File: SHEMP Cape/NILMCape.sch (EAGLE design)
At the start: 26 parts, among them U1 ADS8568_PM_64, U2 ACS756KCA-050B-PFF-T, U3 LTC6082, U4 LTC6082, U5 LM2687_DGK_8

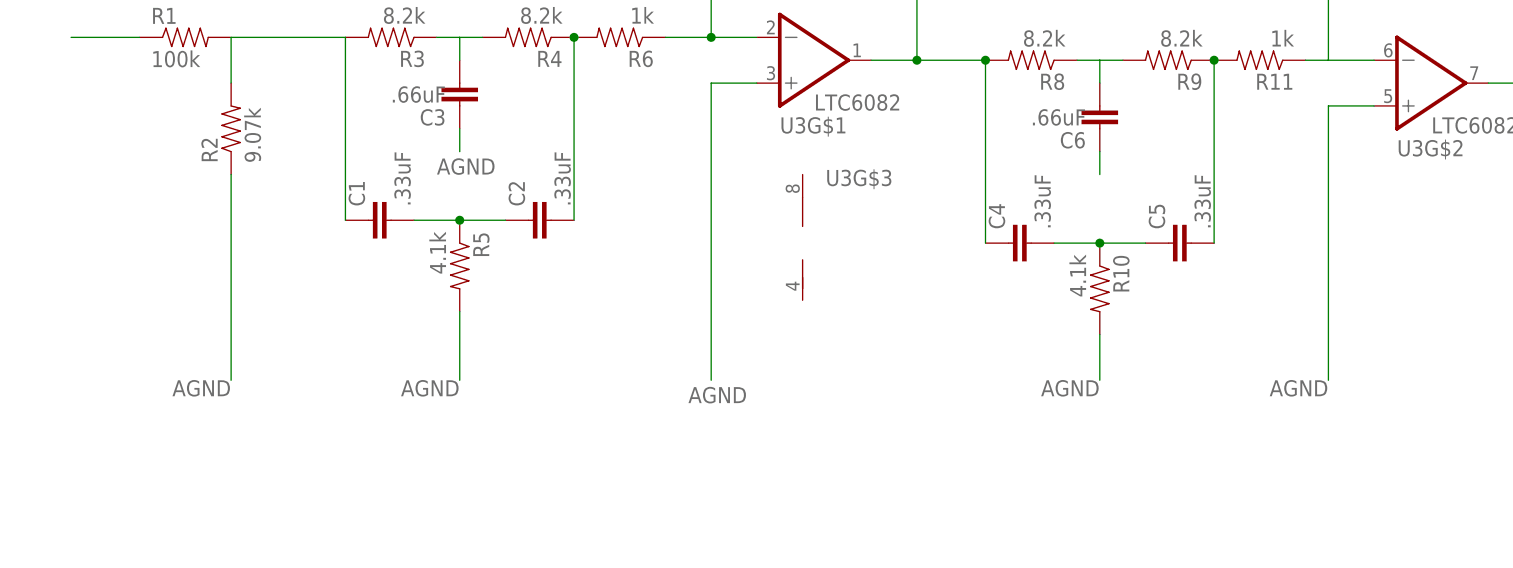
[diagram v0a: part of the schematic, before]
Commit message: Added Frequency Response
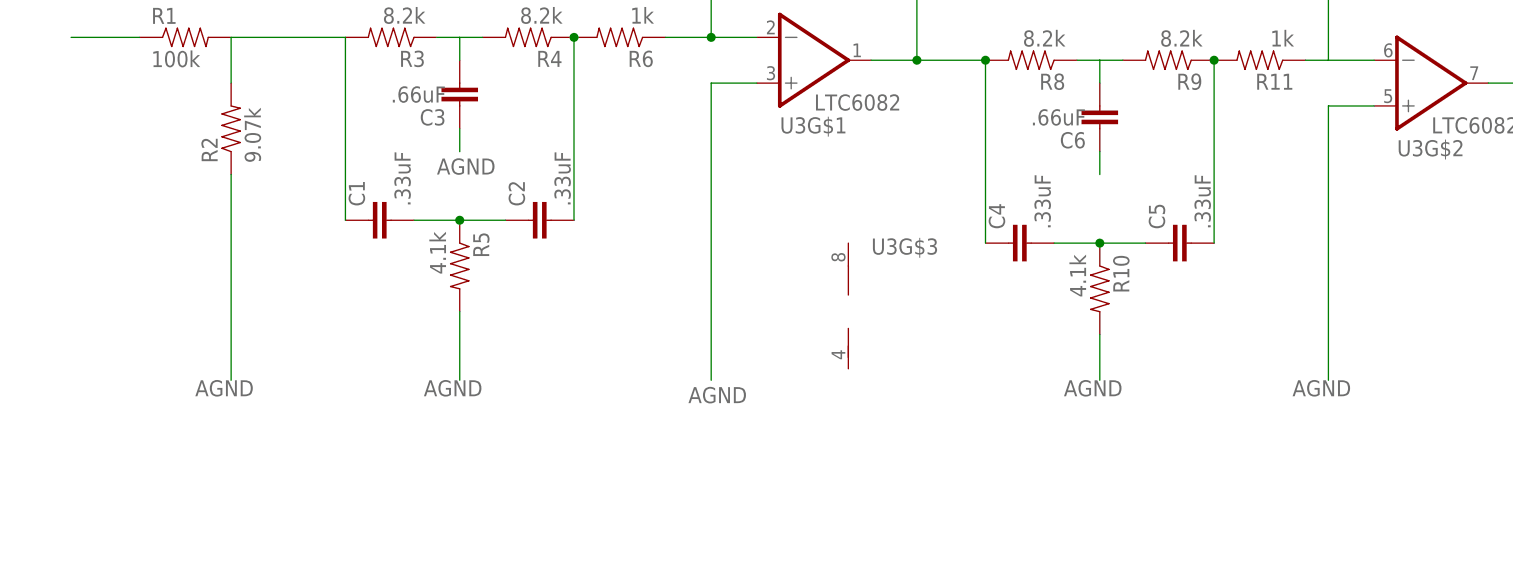
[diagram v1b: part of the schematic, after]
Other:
- moved on the sheet: U3G$3
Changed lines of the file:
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@@
 <?xml version="1.0" encoding="utf-8"?>
 <!DOCTYPE eagle SYSTEM "eagle.dtd">
-<eagle version="6.4">
+<eagle version="6.5.0">
 <drawing>
 <settings>
@@
 <instance part="U3" gate="G$1" x="208.28" y="104.14" rot="MR180"/>
 <instance part="U3" gate="G$2" x="276.86" y="101.6" rot="MR180"/>
-<instance part="U3" gate="G$3" x="208.28" y="83.82"/>
+<instance part="U3" gate="G$3" x="213.36" y="76.2"/>
 <instance part="U2" gate="A" x="38.1" y="223.52"/>
 <instance part="U2" gate="B" x="68.58" y="220.98" rot="R90"/>
@@
 <pinref part="R2" gate="G$1" pin="1"/>
 <wire x1="144.78" y1="91.44" x2="144.78" y2="68.58" width="0.1524" layer="91"/>
-<label x="144.78" y="68.58" size="1.778" layer="95" rot="R180"/>
+<label x="147.32" y="68.58" size="1.778" layer="95" rot="R180"/>
 </segment>
 <segment>
 <pinref part="R5" gate="G$1" pin="2"/>
 <wire x1="170.18" y1="76.2" x2="170.18" y2="68.58" width="0.1524" layer="91"/>
-<label x="170.18" y="68.58" size="1.778" layer="95" rot="R180"/>
+<label x="172.72" y="68.58" size="1.778" layer="95" rot="R180"/>
 </segment>
 <segment>
@@
 <pinref part="R10" gate="G$1" pin="2"/>
 <wire x1="241.3" y1="73.66" x2="241.3" y2="68.58" width="0.1524" layer="91"/>
-<label x="241.3" y="68.58" size="1.778" layer="95" rot="R180"/>
+<label x="243.84" y="68.58" size="1.778" layer="95" rot="R180"/>
 </segment>
 <segment>
@@
 <wire x1="271.78" y1="99.06" x2="266.7" y2="99.06" width="0.1524" layer="91"/>
 <wire x1="266.7" y1="99.06" x2="266.7" y2="68.58" width="0.1524" layer="91"/>
-<label x="266.7" y="68.58" size="1.778" layer="95" rot="R180"/>
-</segment>
-</net>
+<label x="269.24" y="68.58" size="1.778" layer="95" rot="R180"/>
+</segment>
+</net>

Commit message: Split rail work, finished filtering stage.
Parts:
- removed R10: 4.1k, SensorCape:RESISTOR0805-RES
- removed R6: 1k, SensorCape:RESISTOR0805-RES
- added C10, C9: .33uF, SensorCape:CAP0805
- added C7, C8: 1uF, SensorCape:CAP0805
- added R13, R14: 8.2k, SensorCape:RESISTOR0805-RES
- added U$2: TPS84259_RKG_41, SensorCape:TPS84259_RKG_41
- added U$3: TPS7A4700_RGW_20, SensorCape:TPS7A4700_RGW_20
- added U6: TPS7A3301_RGW_20, SensorCape:TPS7A3301_RGW_20
- C3, C6: value .66uF -> .33uF
- R1: value 100k -> 1k
- R11: value 1k -> 15k
- R12: value 20k -> 1k
- R2: value 9.07k -> 8.2k
- R5: value 4.1k -> 8.2k
- R7: value 10k -> 1k
- U3, U4: value LTC6082 -> TLC2272A_D_8; device SensorCape:LTC6082 -> SensorCape:TLC2272A_D_8
- U5: value LM2687_DGK_8 -> TPS84250_RKG_41; device SensorCape:LM2687_DGK_8 -> SensorCape:TPS84250_RKG_41
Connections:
- removed net AVDD: U$1.SYS_5V@1, U$1.SYS_5V@2
- removed net DGND: U$1.GND@1, U$1.GND@2, U$1.GND@3, U$1.GND@4, U$1.GND@5, U$1.GND@6, U$1.GND@7, U$1.GND@8
- removed net DVDD: U$1.VDD_3V3EXP@1, U$1.VDD_3V3EXP@2
- removed net N$1: R1.1
- removed net N$14: C6.2, R8.1, R9.2
- removed net N$5: C2.2, R4.1, R6.2
- new net N$17: C7.1, U3.1IN-, U3.1OUT
- new net N$30: C7.2, R1.2
- new net N$31: R1.1, R7.2, U3.2IN-
- new net N$32: R11.2, R12.1, U4.2IN-
- new net N$33: U4.2OUT
- net AGND: now also C10.1, C4.1, C9.1, R13.2, R14.2, R2.2, U3.2IN+, U4.2IN+; no longer R10.2, R2.1, U3G$1.+IN, U3G$2.+IN
- net HVDD: now also U3.VDD+, U4.VDD+; no longer U$1.VDD_5V@1, U$1.VDD_5V@2
- net HVSS: now also U3.VDD-/GND, U4.VDD-/GND; no longer U5.OUT
- net N$10: now also C5.1, U3.2OUT; no longer C4.1, R7.1, U3G$1.OUT
- net N$11: now also C5.2, C6.1, R13.1, R14.1; no longer R11.1, R12.2, U3G$2.-IN
- net N$13: now also C10.2, C9.2, R8.1, R9.2; no longer C4.2, C5.1, R10.1
- net N$15: now also C6.2, U4.1IN+; no longer C5.2, R11.2
- net N$16: now also C8.1, U4.1IN-, U4.1OUT; no longer C6.1
- net N$18: now also C8.2, R12.2; no longer R12.1, U3G$2.OUT
- net N$2: no longer R1.2, R2.2
- net N$3: now also R2.1
- net N$4: now also C4.2
- net N$9: now also C2.2, R4.1, U3.1IN+; no longer R6.1, R7.2, U3G$1.-IN
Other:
- note added: "This needs to be connected to the AC input"

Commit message: More schematic capture work.
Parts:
- removed U3, U4: TLC2272A_D_8, SensorCape:TLC2272A_D_8
- added C11: 1uF, SensorCape:CAP0805
- added C12: 4.7uF 50V, SensorCape:CAP1210
- added C13: 2.2uF 100V, SensorCape:CAP1210
- added C14: 22uF 100V, ASL:CAP_POLPTH1
- added C15, C16, C17, C18: 22uF 25V, SensorCape:CAP1210
- added R10, R6: 1k, SensorCape:RESISTOR0805-RES
- added R15: 174k, ASL:RESISTOR0805-RES
- added R16: 63.4k, ASL:RESISTOR0805-RES
- added U7: LP2950-33_KVU_3, SensorCape:LP2950-33_KVU_3
- added U9: TL074_PW_14, SensorCape:TL074_PW_14
- C10: value .33uF -> 1uF
- C7: value 1uF -> .33uF
- C8: value 1uF -> 4.7uF 50V; device SensorCape:CAP0805 -> SensorCape:CAP1210
- R1, R7: value 1k -> 8.2k
- R11: value 15k -> 178k; device SensorCape:RESISTOR0805-RES -> ASL:RESISTOR0805-RES
- R12: value 1k -> 0; device SensorCape:RESISTOR0805-RES -> ASL:RESISTOR0805-RES
- R13, R14: value 8.2k -> 1k
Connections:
- net N$2 renamed HOT_IN
- removed net N$15: C6.2, R9.1, U4.1IN+
- removed net N$16: C8.1, U4.1IN-, U4.1OUT
- removed net N$32: R11.2, R12.1, U4.2IN-
- removed net N$33: U4.2OUT
- new net GND: C12.2, C13.2, C14.-, C15.1, C16.1, C17.1, C18.1, C8.2, R11.2, U$2.GND
- new net HVSS_15D: C15.2, C16.2, C17.2, C18.2, U$2.VOUT
- new net N$1: C5.1, R1.2, R6.2, U9.2OUT
- new net N$14: C10.2, U9.3IN-, U9.3OUT
- new net N$34: C11.2, R10.2
- new net N$35: C11.1, U9.1IN-, U9.1OUT
- new net N$36: R15.1, R16.2, U$2.INH/UVLO
- new net N$37: R12.1, R16.1, U$2.A_VOUT
- new net N$5: R10.1, R6.1, U9.2IN-
- new net SIGNAL_TO_AA: R14.1, U9.4OUT
- new net VIN: C12.1, C13.1, C14.+, C8.1, R15.2, U$2.VIN
- net AGND: now also C7.1, R8.2, R9.2, U9.2IN+, U9.4IN+; no longer C10.1, R13.2, R14.2, U3.2IN+, U4.2IN+
- net HVDD: now also U9.VCC+; no longer U3.VDD+, U4.VDD+
- net HVSS: now also U9.VCC-; no longer U3.VDD-/GND, U4.VDD-/GND
- net N$10: now also C5.2, C6.1, R8.1, R9.1; no longer C5.1, R8.2, U3.2OUT
- net N$11: now also C7.2, C9.2, R1.1, R7.2; no longer C5.2, C6.1, R13.1, R14.1
- net N$13: now also C6.2, R7.1, U9.3IN+; no longer C10.2, C9.2, R8.1, R9.2
- net N$17: now also R13.2, R14.2, U9.4IN-; no longer C7.1, U3.1IN-, U3.1OUT
- net N$18: now also R11.1, U$2.VADJ; no longer C8.2, R12.2
- net N$30: now also C10.1, R13.1; no longer C7.2, R1.2
- net N$31: now also R12.2, U$2.RT; no longer R1.1, R7.2, U3.2IN-
- net N$9: now also U9.1IN+; no longer U3.1IN+
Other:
- note added: "60Hz Filter"
- note added: "SPLIT RAIL CLEAN/DIRTY AND LOGIC VOLTAGE SUPPLY"
- note removed: "This needs to be connected to the AC input"

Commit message: More schematic capture work.
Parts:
- added C19, C26, C31: 10nF, SensorCape:CAP0805
- added C20, C23, C25: 22uF, SensorCape:CAP1210
- added C21, C22, C24: 2.2uF 100V, SensorCape:CAP1210
- added C27: 27uF 100V, SensorCape:CAP_POLPTH1
- added C28, C30: 1uF, SensorCape:CAP0805
- added C29, C32: 47uF, SensorCape:CAP1210
- added C33: 10uF, SensorCape:CAP_POLPTH2
- added C34, C35, C36, C37, C38, C39, C40, C41, C42, C43, C44, C45: .1uF, SensorCape:CAP0805
- added R17, R18: 178k, ASL:RESISTOR0805-RES
- added R19: 174k, ASL:RESISTOR0805-RES
- added R20: 15.8k, ASL:RESISTOR0805-RES
- added R21, R22: 0, ASL:RESISTOR0805-RES
- added R23: 1.5M, ASL:RESISTOR0805-RES
- added R24: 162k, ASL:RESISTOR0805-RES
- added U10, U11, U12, U13, U3, U8: SI8663BC-B-IS1, SensorCape:SI8663BC-B-IS1
- added U14, U4: SN74CBT16390_DGG, SensorCape:SN74CBT16390_DGG
- R16: value 63.4k -> 15.8k
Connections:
- new net ADC_DB0: U1.DB0/DCIN_D, U14.A1
- new net ADC_DB1: U1.DB1/DCIN_C, U14.A2
- new net ADC_DB10: U1.DB10/SCLK, U14.A11
- new net ADC_DB11: U1.DB11/*REFBUFEN, U14.A12
- new net ADC_DB12: U1.DB12/SDO_A, U14.A13
- new net ADC_DB13: U1.DB13/SDO_B, U14.A14
- new net ADC_DB14: U1.DB14/SDO_C, U14.A15
- new net ADC_DB15: U1.DB15/SDO_D, U14.A16
- new net ADC_DB2: U1.DB2/DCIN_B, U14.A3
- new net ADC_DB3: U1.DB3/DCIN_A, U14.A4
- new net ADC_DB4: U1.DB4, U14.A5
- new net ADC_DB5: U1.DB5/SEL_CD, U14.A6
- new net ADC_DB6: U1.DB6/SEL_B, U14.A7
- new net ADC_DB7: U1.DB7, U14.A8
- new net ADC_DB8: U1.DB8/DCEN, U14.A9
- new net ADC_DB9: U1.DB9/SDI, U14.A10
- new net BB_DB0: U4.A1
- new net BB_DB1: U4.A2
- new net BB_DB10: U4.A11
- new net BB_DB11: U4.A12
- new net BB_DB12: U4.A13
- new net BB_DB13: U4.A14
- new net BB_DB14: U4.A15
- new net BB_DB15: U4.A16
- new net BB_DB2: U4.A3
- new net BB_DB3: U4.A4
- new net BB_DB4: U4.A5
- new net BB_DB5: U4.A6
- new net BB_DB6: U4.A7
- new net BB_DB7: U4.A8
- new net BB_DB8: U4.A9
- new net BB_DB9: U4.A10
- new net HVDD_12A: C29.1, U$3.OUT, U$3.OUT_1, U$3.SENSE/FB
- new net HVDD_15D: C20.2, C23.2, C25.2, R17.2, U$3.EN, U$3.IN, U$3.IN_2, U5.VOUT, U7.INPUT
- new net HVSS_12A: C31.1, C32.1, R23.2, U6.OUT, U6.OUT_2
- new net N$100: U$1.SPI1_SCLK
- new net N$15: C19.1, U$2.SS
- new net N$16: C31.2, R24.2, U6.FB
- new net N$2: C20.1, C21.2, C22.2, C23.1, C24.2, C25.1, C27.-, R21.2, U5.AGND, U5.PGND
- new net N$32: C12.2, C13.2, C14.-, C15.1, C16.1, C17.1, C18.1, C8.2, R11.2, R22.2, U$2.GND
- new net N$33: C30.1, U6.NR/SS
- new net N$38: R18.2, U5.RT/CLK
- new net N$39: U$1.GPIO2_22
- new net N$40: U$1.GPIO2_23
- new net N$41: R19.1, R20.2, U5.INH/UVLO
- new net N$42: U$1.GPIO2_24
- new net N$43: C26.1, U5.SS/TR
- new net N$44: C26.2, R18.1, R20.1, R21.1, U5.GND_PT, U5.STSEL
- new net N$45: C28.1, U$3.NR
- new net N$46: U$1.GPIO2_25
- new net N$47: U$1.UART5_CTSN
- new net N$48: U$1.UART4_RTSN
- new net N$49: U$1.UART4_CTSN
- new net N$50: U$1.UART5_TXD
- new net N$51: U$1.UART5_RTSN
- new net N$52: U$1.UART3_RTSN
- new net N$53: U$1.UART3_CTSN
- new net N$54: U$1.UART5_RXD
- new net N$55: U$1.GPIO2_6
- new net N$56: U$1.GPIO2_7
- new net N$57: U$1.GPIO2_8
- new net N$58: U$1.GPIO2_9
- new net N$59: U$1.GPIO2_10
- new net N$60: U$1.GPIO2_11
- new net N$61: U$1.GPIO2_12
- new net N$62: U$1.GPIO2_13
- new net N$63: U$1.GPIO1_13
- new net N$64: U$1.GPIO1_12
- new net N$65: C44.1
- new net N$66: C34.1
- new net N$67: U$1.EHRPWM2B
- new net N$68: U$1.GPIO0_26
- new net N$69: U$1.GPIO1_15
- new net N$70: U$1.GPIO1_14
- new net N$71: U$1.GPIO0_27
- new net N$72: U$1.EHRPWM2A
- new net N$73: U$1.GPIO1_31
- new net N$74: U$1.GPIO1_30
- new net N$75: U$1.GPIO2_1
- new net N$76: U$1.GPIO1_5
- new net N$77: U$1.TIMER4
- new net N$78: U$1.GPIO1_6
- new net N$79: U$1.GPIO1_2
- new net N$80: U$1.GPIO1_7
- new net N$81: U$1.GPIO1_3
- new net N$82: U$1.GPIO1_1
- new net N$83: U$1.GPIO1_29
- new net N$84: U$1.GPIO1_4
- new net N$85: U$1.GPIO1_0
- new net N$86: U$1.GPIO1_28
- new net N$87: U$1.GPIO3_19
- new net N$88: U$1.GPIO3_21
- new net N$89: U$1.GPIO1_17
- new net N$90: U$1.TIMER5
- new net N$91: U$1.TIMER7
- new net N$92: U$1.TIMER6
- new net N$93: U$1.GPIO1_16
- new net N$94: U$1.GPIO0_7
- new net N$95: U$1.UART2_TXD
- new net N$96: U$1.UART2_RXD
- new net N$97: U$1.UART4_RXD
- new net N$98: U$1.UART4_TXD
- new net N$99: U$1.SPI1_DO
- new net R_DB0: U12.B1, U4.1B1
- new net R_DB1: U12.B2, U4.1B2
- new net R_DB10: U3.B2, U4.1B11
- new net R_DB11: U3.B3, U4.1B12
- new net R_DB12: U4.1B13, U8.B1
- new net R_DB13: U4.1B14, U8.B2
- new net R_DB14: U4.1B15, U8.B3
- new net R_DB15: U13.B1, U4.1B16
- new net R_DB2: U12.B3, U4.1B3
- new net R_DB3: U11.B1, U4.1B4
- new net R_DB4: U11.B2, U4.1B5
- new net R_DB5: U11.B3, U4.1B6
- new net R_DB6: U10.B1, U4.1B7
- new net R_DB7: U10.B2, U4.1B8
- new net R_DB8: U10.B3, U4.1B9
- new net R_DB9: U3.B1, U4.1B10
- new net R_DB_ADC0: U12.A4, U14.1B1
- new net R_DB_ADC1: U12.A5, U14.1B2
- new net R_DB_ADC10: U14.1B11, U3.A5
- new net R_DB_ADC11: U14.1B12, U3.A6
- new net R_DB_ADC12: U14.1B13, U8.A4
- new net R_DB_ADC13: U14.1B14, U8.A5
- new net R_DB_ADC14: U14.1B15, U8.A6
- new net R_DB_ADC15: U13.A4, U14.1B16
- new net R_DB_ADC2: U12.A6, U14.1B3
- new net R_DB_ADC3: U11.A4, U14.1B4
- new net R_DB_ADC4: U11.A5, U14.1B5
- new net R_DB_ADC5: U11.A6, U14.1B6
- new net R_DB_ADC6: U10.A4, U14.1B7
- new net R_DB_ADC7: U10.A5, U14.1B8
- new net R_DB_ADC8: U10.A6, U14.1B9
- new net R_DB_ADC9: U14.1B10, U3.A4
- new net VDD3V3_D: C33.+, C34.2, C35.2, C36.2, C37.2, C38.2, C39.2, C40.2, C41.2, C42.2, C43.2, C44.2, C45.2, U10.VDD1, U10.VDD2, U11.VDD1, U11.VDD2, U12.VDD1, U12.VDD2, U13.VDD1, U13.VDD2, U3.VDD1, U3.VDD2, U7.OUTPUT, U8.VDD1, U8.VDD2
- new net W_DB0: U12.B4, U4.2B1
- new net W_DB1: U12.B5, U4.2B2
- new net W_DB10: U3.B5, U4.2B11
- new net W_DB11: U3.B6, U4.2B12
- new net W_DB12: U4.2B13, U8.B4
- new net W_DB13: U4.2B14, U8.B5
- new net W_DB14: U4.2B15, U8.B6
- new net W_DB15: U13.B4, U4.2B16
- new net W_DB2: U12.B6, U4.2B3
- new net W_DB3: U11.B4, U4.2B4
- new net W_DB4: U11.B5, U4.2B5
- new net W_DB5: U11.B6, U4.2B6
- new net W_DB6: U10.B4, U4.2B7
- new net W_DB7: U10.B5, U4.2B8
- new net W_DB8: U10.B6, U4.2B9
- new net W_DB9: U3.B4, U4.2B10
- new net W_DB_ADC0: U12.A1, U14.2B1
- new net W_DB_ADC1: U12.A2, U14.2B2
- new net W_DB_ADC10: U14.2B11, U3.A2
- new net W_DB_ADC11: U14.2B12, U3.A3
- new net W_DB_ADC12: U14.2B13, U8.A1
- new net W_DB_ADC13: U14.2B14, U8.A2
- new net W_DB_ADC14: U14.2B15, U8.A3
- new net W_DB_ADC15: U13.A1, U14.2B16
- new net W_DB_ADC2: U12.A3, U14.2B3
- new net W_DB_ADC3: U11.A1, U14.2B4
- new net W_DB_ADC4: U11.A2, U14.2B5
- new net W_DB_ADC5: U14.2B6
- new net W_DB_ADC6: U10.A1, U11.A3, U14.2B7
- new net W_DB_ADC7: U10.A2, U14.2B8
- new net W_DB_ADC8: U10.A3, U14.2B9
- new net W_DB_ADC9: U14.2B10, U3.A1
- net GND: now also C19.2, C28.2, C29.2, C30.2, C32.2, C33.-, C35.1, C36.1, C37.1, C38.1, C39.1, C40.1, C41.1, C42.1, C43.1, C45.1, R12.1, R16.1, R22.1, R24.1, U$2.A_VOUT, U$2.VOUT_PT, U$3.0P2V, U$3.0P8V, U$3.3P2V, U$3.6P4V2, U$3.EPAD, U$3.GND, U10.GND1, U10.GND2, U11.GND1, U11.GND2, U12.GND1, U12.GND2, U13.GND1, U13.GND2, U3.GND1, U3.GND2, U6.EPAD, U6.GND, U7.GND, U8.GND1, U8.GND2; no longer C12.2, C13.2, C14.-, C15.1, C16.1, C17.1, C18.1, C8.2, R11.2, U$2.GND
- net HVSS_15D: now also U6.EN, U6.IN, U6.IN_2
- net N$37: now also R17.1, U5.VADJ; no longer R12.1, R16.1, U$2.A_VOUT
- net VIN: now also C21.1, C22.1, C24.1, C27.+, R19.2, U5.VIN
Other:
- note added: "BeagleBone Header Interface"
- note added: "Digital Isolation"
- note added: "Digital Pot Goes Here"
- note added: "LCD"
- note added: "eMMC"

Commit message: More schematic capture work.
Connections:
- removed net N$100: U$1.SPI1_SCLK
- removed net N$86: U$1.GPIO1_28
- removed net N$87: U$1.GPIO3_19
- removed net N$88: U$1.GPIO3_21
- removed net N$89: U$1.GPIO1_17
- removed net N$93: U$1.GPIO1_16
- removed net N$94: U$1.GPIO0_7
- removed net N$95: U$1.UART2_TXD
- removed net N$96: U$1.UART2_RXD
- removed net N$97: U$1.UART4_RXD
- removed net N$98: U$1.UART4_TXD
- removed net N$99: U$1.SPI1_DO
- net BB_DB0: now also U$1.UART4_RXD
- net BB_DB1: now also U$1.UART4_TXD
- net BB_DB10: now also U$1.EHRPWM1A
- net BB_DB11: now also U$1.EHRPWM1B
- net BB_DB12: now also U$1.UART2_RXD
- net BB_DB13: now also U$1.UART1_TXD
- net BB_DB14: now also U$1.UART1_RXD
- net BB_DB15: now also U$1.GPIO0_7
- net BB_DB2: now also U$1.GPIO1_16
- net BB_DB3: now also U$1.UART2_TXD
- net BB_DB4: now also U$1.GPIO1_17
- net BB_DB5: now also U$1.GPIO3_21
- net BB_DB6: now also U$1.GPIO3_19
- net BB_DB7: now also U$1.SPI1_DO
- net BB_DB8: now also U$1.SPI1_SCLK
- net BB_DB9: now also U$1.GPIO1_28
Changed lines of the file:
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@@
 </instances>
 <busses>
+<bus name="BB_DB[0..15]">
+<segment>
+<wire x1="154.94" y1="137.16" x2="154.94" y2="106.68" width="0.762" layer="92"/>
+<label x="154.94" y="137.16" size="1.778" layer="95" rot="R90"/>
+</segment>
+<segment>
+<wire x1="266.7" y1="137.16" x2="266.7" y2="93.98" width="0.762" layer="92"/>
+<label x="266.7" y="137.16" size="1.778" layer="95" rot="R90"/>
+</segment>
+</bus>
 </busses>
 <nets>
@@
 </segment>
 </net>
-<net name="N$86" class="0">
-<segment>
-<pinref part="U$1" gate="G$1" pin="GPIO1_28"/>
-<wire x1="243.84" y1="134.62" x2="259.08" y2="134.62" width="0.1524" layer="91"/>
-</segment>
-</net>
-<net name="N$87" class="0">
-<segment>
-<pinref part="U$1" gate="G$1" pin="GPIO3_19"/>
-<wire x1="187.96" y1="114.3" x2="175.26" y2="114.3" width="0.1524" layer="91"/>
-</segment>
-</net>
-<net name="N$88" class="0">
-<segment>
-<pinref part="U$1" gate="G$1" pin="GPIO3_21"/>
-<wire x1="187.96" y1="116.84" x2="175.26" y2="116.84" width="0.1524" layer="91"/>
-</segment>
-</net>
-<net name="N$89" class="0">
-<segment>
-<pinref part="U$1" gate="G$1" pin="GPIO1_17"/>
-<wire x1="187.96" y1="119.38" x2="175.26" y2="119.38" width="0.1524" layer="91"/>
-</segment>
-</net>
 <net name="N$77" class="0">
 <segment>
@@
 </segment>
 </net>
-<net name="N$93" class="0">
+<net name="BB_DB0" class="0">
+<segment>
+<pinref part="U$1" gate="G$1" pin="UART4_RXD"/>
+<wire x1="154.94" y1="134.62" x2="187.96" y2="134.62" width="0.1524" layer="91"/>
+</segment>
+</net>
+<net name="BB_DB1" class="0">
+<segment>
+<pinref part="U$1" gate="G$1" pin="UART4_TXD"/>
+<wire x1="154.94" y1="132.08" x2="187.96" y2="132.08" width="0.1524" layer="91"/>
+</segment>
+</net>
+<net name="BB_DB2" class="0">
 <segment>
 <pinref part="U$1" gate="G$1" pin="GPIO1_16"/>
-<wire x1="187.96" y1="129.54" x2="175.26" y2="129.54" width="0.1524" layer="91"/>
-</segment>
-</net>
-<net name="N$94" class="0">
+<wire x1="154.94" y1="129.54" x2="187.96" y2="129.54" width="0.1524" layer="91"/>
+</segment>
+</net>
+<net name="BB_DB3" class="0">
+<segment>
+<pinref part="U$1" gate="G$1" pin="UART2_TXD"/>
+<wire x1="154.94" y1="121.92" x2="187.96" y2="121.92" width="0.1524" layer="91"/>
+</segment>
+</net>
+<net name="BB_DB4" class="0">
+<segment>
+<pinref part="U$1" gate="G$1" pin="GPIO1_17"/>
+<wire x1="154.94" y1="119.38" x2="187.96" y2="119.38" width="0.1524" layer="91"/>
+</segment>
+</net>
+<net name="BB_DB5" class="0">
+<segment>
+<pinref part="U$1" gate="G$1" pin="GPIO3_21"/>
+<wire x1="154.94" y1="116.84" x2="187.96" y2="116.84" width="0.1524" layer="91"/>
+</segment>
+</net>
+<net name="BB_DB6" class="0">
+<segment>
+<pinref part="U$1" gate="G$1" pin="GPIO3_19"/>
+<wire x1="154.94" y1="114.3" x2="187.96" y2="114.3" width="0.1524" layer="91"/>
+</segment>
+</net>
+<net name="BB_DB7" class="0">
+<segment>
+<pinref part="U$1" gate="G$1" pin="SPI1_DO"/>
+<wire x1="154.94" y1="111.76" x2="187.96" y2="111.76" width="0.1524" layer="91"/>
+</segment>
+</net>
+<net name="BB_DB8" class="0">
+<segment>
+<pinref part="U$1" gate="G$1" pin="SPI1_SCLK"/>
+<wire x1="154.94" y1="109.22" x2="187.96" y2="109.22" width="0.1524" layer="91"/>
+</segment>
+</net>
+<net name="BB_DB9" class="0">
+<segment>
+<pinref part="U$1" gate="G$1" pin="GPIO1_28"/>
+<wire x1="243.84" y1="134.62" x2="266.7" y2="134.62" width="0.1524" layer="91"/>
+</segment>
+</net>
+<net name="BB_DB10" class="0">
+<segment>
+<pinref part="U$1" gate="G$1" pin="EHRPWM1A"/>
+<wire x1="243.84" y1="132.08" x2="266.7" y2="132.08" width="0.1524" layer="91"/>
+</segment>
+</net>
+<net name="BB_DB11" class="0">
+<segment>
+<pinref part="U$1" gate="G$1" pin="EHRPWM1B"/>
+<wire x1="243.84" y1="129.54" x2="266.7" y2="129.54" width="0.1524" layer="91"/>
+</segment>
+</net>
+<net name="BB_DB12" class="0">
+<segment>
+<pinref part="U$1" gate="G$1" pin="UART2_RXD"/>
+<wire x1="243.84" y1="121.92" x2="266.7" y2="121.92" width="0.1524" layer="91"/>
+</segment>
+</net>
+<net name="BB_DB13" class="0">
+<segment>
+<pinref part="U$1" gate="G$1" pin="UART1_TXD"/>
+<wire x1="243.84" y1="119.38" x2="266.7" y2="119.38" width="0.1524" layer="91"/>
+</segment>
+</net>
+<net name="BB_DB14" class="0">
+<segment>
+<pinref part="U$1" gate="G$1" pin="UART1_RXD"/>
+<wire x1="243.84" y1="116.84" x2="266.7" y2="116.84" width="0.1524" layer="91"/>
+</segment>
+</net>
+<net name="BB_DB15" class="0">
 <segment>
 <pinref part="U$1" gate="G$1" pin="GPIO0_7"/>
-<wire x1="243.84" y1="96.52" x2="259.08" y2="96.52" width="0.1524" layer="91"/>
-</segment>
-</net>
-<net name="N$95" class="0">
-<segment>
-<pinref part="U$1" gate="G$1" pin="UART2_TXD"/>
-<wire x1="187.96" y1="121.92" x2="175.26" y2="121.92" width="0.1524" layer="91"/>
-</segment>
-</net>
-<net name="N$96" class="0">
-<segment>
-<pinref part="U$1" gate="G$1" pin="UART2_RXD"/>
-<wire x1="243.84" y1="121.92" x2="259.08" y2="121.92" width="0.1524" layer="91"/>
-</segment>
-</net>
-<net name="N$97" class="0">
-<segment>
-<pinref part="U$1" gate="G$1" pin="UART4_RXD"/>
-<wire x1="187.96" y1="134.62" x2="175.26" y2="134.62" width="0.1524" layer="91"/>
-</segment>
-</net>
-<net name="N$98" class="0">
-<segment>
-<pinref part="U$1" gate="G$1" pin="UART4_TXD"/>
-<wire x1="187.96" y1="132.08" x2="175.26" y2="132.08" width="0.1524" layer="91"/>
-</segment>
-</net>
-<net name="N$99" class="0">
-<segment>
-<pinref part="U$1" gate="G$1" pin="SPI1_DO"/>
-<wire x1="187.96" y1="111.76" x2="175.26" y2="111.76" width="0.1524" layer="91"/>
-</segment>
-</net>
-<net name="N$100" class="0">
-<segment>
-<pinref part="U$1" gate="G$1" pin="SPI1_SCLK"/>
-<wire x1="187.96" y1="109.22" x2="175.26" y2="109.22" width="0.1524" layer="91"/>
-</segment>
-</net>
+<wire x1="243.84" y1="96.52" x2="266.7" y2="96.52" width="0.1524" layer="91"/>
+</segment>
+</net>
